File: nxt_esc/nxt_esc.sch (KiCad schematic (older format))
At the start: 15 parts, among them IC1 L293D, J1 NXT_MOTOR, J2 NXT_MOTOR, SW1 Skid Steer/Drive & Steer, U1 LM7809CT

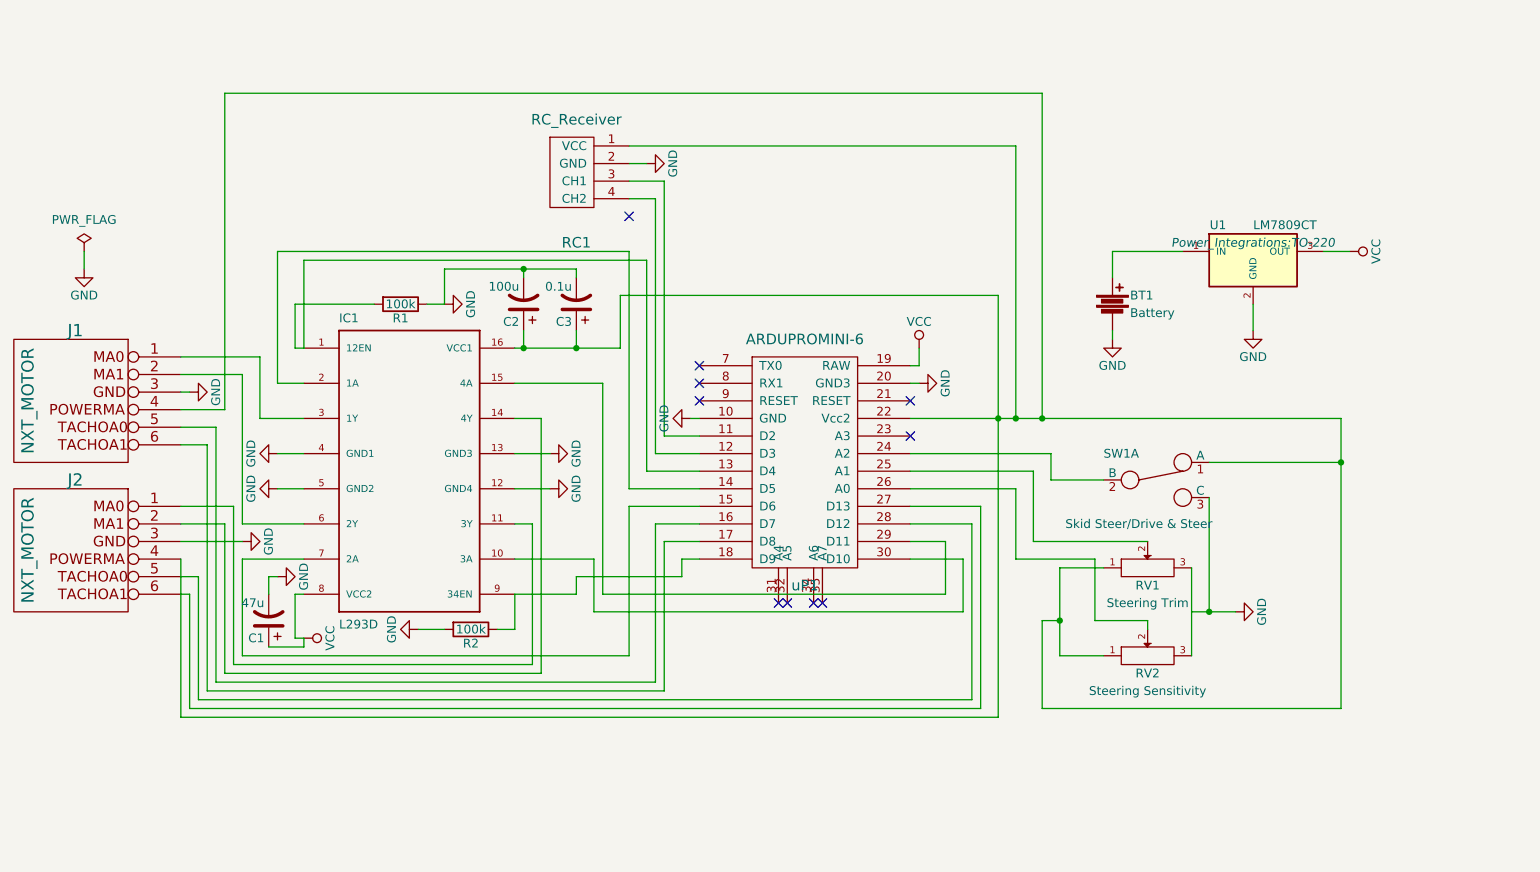
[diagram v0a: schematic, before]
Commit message: Changed schematic
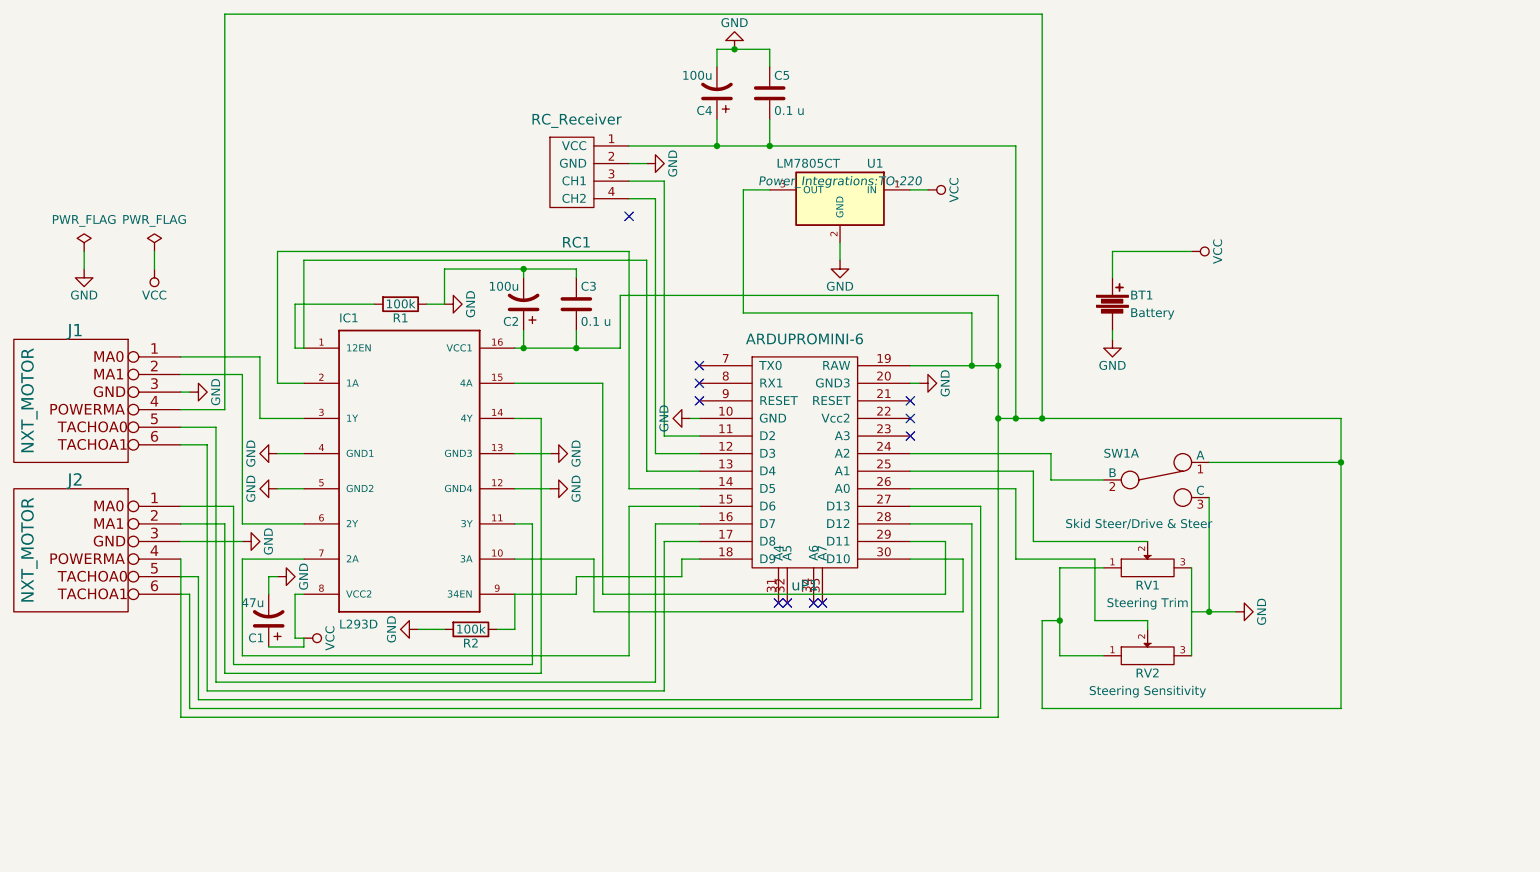
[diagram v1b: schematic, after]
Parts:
- removed C3: 0.1u, Capacitors_ThroughHole:C_Disc_D3.4mm_W2.1mm_P2.50mm, symbol CP1
- removed U1: LM7809CT, Power_Integrations:TO-220, symbol LM7809CT
- added C3, C5: 0.1 u, Capacitors_ThroughHole:C_Disc_D3.4mm_W2.1mm_P2.50mm, symbol C
- added C4: 100u, Capacitors_ThroughHole:CP_Radial_D5.0mm_P2.50mm, symbol CP1
- added U1: LM7805CT, Power_Integrations:TO-220, symbol LM7805CT
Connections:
- net GND: now also C3.1, C4.2, C5.1, U1.2 (GND)
- net VCC: now also BT1.1, U1.1 (IN); no longer uP1.19 (RAW)
- net at C2.1, IC1.16 (VCC1), J1.4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: now also uP1.19 (RAW), C3.2, C4.1, C5.2, U1.3 (OUT); no longer uP1.22 (Vcc2)
- no-connect marks 10 -> 11
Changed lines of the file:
@@
-$EndComp
-$Comp
-L VCC #PWR013
-U 1 1 5A555AFB
-P 6950 3000
-F 0 "#PWR013" H 6950 2850 50  0001 C CNN
-F 1 "VCC" H 6950 3150 50  0000 C CNN
-F 2 "" H 6950 3000 50  0000 C CNN
-F 3 "" H 6950 3000 50  0000 C CNN
-	1    6950 3000
-	1    0    0    -1
 $EndComp
 $Comp
@@
 $EndComp
 $Comp
-L GND #PWR014
+L GND #PWR013
 U 1 1 5A554FA2
 P 4250 2750
-F 0 "#PWR014" H 4250 2500 50  0001 C CNN
+F 0 "#PWR013" H 4250 2500 50  0001 C CNN
 F 1 "GND" H 4250 2600 50  0000 C CNN
 F 2 "" H 4250 2750 50  0000 C CNN
@@
 $EndComp
 $Comp
-L GND #PWR015
+L GND #PWR014
 U 1 1 5A5551A8
 P 4100 4600
-F 0 "#PWR015" H 4100 4350 50  0001 C CNN
+F 0 "#PWR014" H 4100 4350 50  0001 C CNN
 F 1 "GND" H 4100 4450 50  0000 C CNN
 F 2 "" H 4100 4600 50  0000 C CNN
@@
 $EndComp
 $Comp
-L GND #PWR016
+L GND #PWR015
 U 1 1 5A5557E8
 P 3300 4300
-F 0 "#PWR016" H 3300 4050 50  0001 C CNN
+F 0 "#PWR015" H 3300 4050 50  0001 C CNN
 F 1 "GND" H 3300 4150 50  0000 C CNN
 F 2 "" H 3300 4300 50  0000 C CNN
@@
 	-1   0    0    1
 $EndComp
-$Comp
-L CP1 C3
-U 1 1 5A555C2B
-P 5000 2750
-F 0 "C3" H 5025 2850 50  0000 L CNN
-F 1 "0.1u" H 5025 2650 50  0000 L CNN
-F 2 "Capacitors_ThroughHole:C_Disc_D3.4mm_W2.1mm_P2.50mm" H 5000 2750 50  0001 C CNN
-F 3 "" H 5000 2750 50  0000 C CNN
-	1    5000 2750
-	-1   0    0    1
-$EndComp
 Wire Wire Line
 	3450 3200 3300 3200
@@
 	3400 4400 3400 4650
 Wire Wire Line
-	6900 3100 6950 3100
-Wire Wire Line
-	6950 3100 6950 3000
-Wire Wire Line
 	2750 3350 3000 3350
 Wire Wire Line
-	3000 3350 3000 1550
-Wire Wire Line
-	3000 1550 7650 1550
-Wire Wire Line
-	7650 1550 7650 3400
+	3000 3350 3000 1100
+Wire Wire Line
+	3000 1100 7650 1100
+Wire Wire Line
+	7650 1100 7650 3400
 Wire Wire Line
 	2750 4200 2750 5100
@@
 Wire Wire Line
 	7400 2700 7400 5100
-Wire Wire Line
-	6900 3400 9350 3400
 Connection ~ 7400 3400
 Connection ~ 7500 3400
@@
 Connection ~ 4700 2550
 $Comp
-L LM7809CT U1
-U 1 1 5A556A7B
-P 8850 2500
-F 0 "U1" H 8650 2700 50  0000 C CNN
-F 1 "LM7809CT" H 8850 2700 50  0000 L CNN
-F 2 "Power_Integrations:TO-220" H 8850 2600 50  0000 C CIN
-F 3 "" H 8850 2500 50  0000 C CNN
-	1    8850 2500
-	1    0    0    -1
-$EndComp
-$Comp
-L VCC #PWR017
+L VCC #PWR016
 U 1 1 5A556AED
-P 9400 2450
-F 0 "#PWR017" H 9400 2300 50  0001 C CNN
-F 1 "VCC" H 9400 2600 50  0000 C CNN
-F 2 "" H 9400 2450 50  0000 C CNN
-F 3 "" H 9400 2450 50  0000 C CNN
-	1    9400 2450
+P 8500 2450
+F 0 "#PWR016" H 8500 2300 50  0001 C CNN
+F 1 "VCC" H 8500 2600 50  0000 C CNN
+F 2 "" H 8500 2450 50  0000 C CNN
+F 3 "" H 8500 2450 50  0000 C CNN
+	1    8500 2450
 	0    1    1    0
 $EndComp
-$Comp
-L GND #PWR018
-U 1 1 5A556B19
-P 8850 2900
-F 0 "#PWR018" H 8850 2650 50  0001 C CNN
-F 1 "GND" H 8850 2750 50  0000 C CNN
-F 2 "" H 8850 2900 50  0000 C CNN
-F 3 "" H 8850 2900 50  0000 C CNN
-	1    8850 2900
-	-1   0    0    -1
-$EndComp
-Wire Wire Line
-	8850 2750 8850 2900
-Wire Wire Line
-	9250 2450 9400 2450
 $Comp
 L Battery BT1
@@
 	1    0    0    -1
 $EndComp
-Wire Wire Line
-	8050 2600 8050 2450
-Wire Wire Line
-	8050 2450 8450 2450
-$Comp
-L GND #PWR019
+$Comp
+L GND #PWR017
 U 1 1 5A556F7B
 P 8050 2950
-F 0 "#PWR019" H 8050 2700 50  0001 C CNN
+F 0 "#PWR017" H 8050 2700 50  0001 C CNN
 F 1 "GND" H 8050 2800 50  0000 C CNN
 F 2 "" H 8050 2950 50  0000 C CNN
@@
 $EndComp
 $Comp
-L GND #PWR020
+L GND #PWR018
 U 1 1 5A55820D
 P 8750 4500
-F 0 "#PWR020" H 8750 4250 50  0001 C CNN
+F 0 "#PWR018" H 8750 4250 50  0001 C CNN
 F 1 "GND" H 8750 4350 50  0000 C CNN
 F 2 "" H 8750 4500 50  0000 C CNN
@@
 Connection ~ 9350 3650
 Connection ~ 7650 3400
+Wire Wire Line
+	8050 2600 8050 2450
+Wire Wire Line
+	8050 2450 8500 2450
+$Comp
+L LM7805CT U1
+U 1 1 5A56A755
+P 6500 2150
+F 0 "U1" H 6300 2350 50  0000 C CNN
+F 1 "LM7805CT" H 6500 2350 50  0000 L CNN
+F 2 "Power_Integrations:TO-220" H 6500 2250 50  0000 C CIN
+F 3 "" H 6500 2150 50  0000 C CNN
+	1    6500 2150
+	-1   0    0    -1
+$EndComp
+$Comp
+L GND #PWR019
+U 1 1 5A56A814
+P 6500 2500
+F 0 "#PWR019" H 6500 2250 50  0001 C CNN
+F 1 "GND" H 6500 2350 50  0000 C CNN
+F 2 "" H 6500 2500 50  0000 C CNN
+F 3 "" H 6500 2500 50  0000 C CNN
+	1    6500 2500
+	-1   0    0    -1
+$EndComp
+Wire Wire Line
+	6500 2400 6500 2500
+$Comp
+L VCC #PWR020
+U 1 1 5A56A933
+P 7000 2100
+F 0 "#PWR020" H 7000 1950 50  0001 C CNN
+F 1 "VCC" H 7000 2250 50  0000 C CNN
+F 2 "" H 7000 2100 50  0000 C CNN
+F 3 "" H 7000 2100 50  0000 C CNN
+	1    7000 2100
+	0    1    1    0
+$EndComp
+Wire Wire Line
+	6900 2100 7000 2100
+Wire Wire Line
+	6900 3100 7400 3100
+Wire Wire Line
+	5950 2800 5950 2100
+Wire Wire Line
+	5950 2100 6100 2100
+Wire Wire Line
+	5950 2800 7250 2800
+Wire Wire Line
+	7250 2800 7250 3100
+Wire Wire Line
+	9350 3400 7400 3400
+NoConn ~ 6900 3400
+Connection ~ 7400 3100
+Connection ~ 7250 3100
+$Comp
+L PWR_FLAG #FLG021
+U 1 1 5A56B6A2
+P 2600 2450
+F 0 "#FLG021" H 2600 2545 50  0001 C CNN
+F 1 "PWR_FLAG" H 2600 2630 50  0000 C CNN
+F 2 "" H 2600 2450 50  0000 C CNN
+F 3 "" H 2600 2450 50  0000 C CNN
+	1    2600 2450
+	1    0    0    -1
+$EndComp
+$Comp
+L VCC #PWR022
+U 1 1 5A56B6DA
+P 2600 2550
+F 0 "#PWR022" H 2600 2400 50  0001 C CNN
+F 1 "VCC" H 2600 2700 50  0000 C CNN
+F 2 "" H 2600 2550 50  0000 C CNN
+F 3 "" H 2600 2550 50  0000 C CNN
+	1    2600 2550
+	-1   0    0    1
+$EndComp
+Wire Wire Line
+	2600 2450 2600 2550
+$Comp
+L CP1 C4
+U 1 1 5A56BDA4
+P 5800 1550
+F 0 "C4" H 5825 1650 50  0000 L CNN
+F 1 "100u" H 5825 1450 50  0000 L CNN
+F 2 "Capacitors_ThroughHole:CP_Radial_D5.0mm_P2.50mm" H 5800 1550 50  0001 C CNN
+F 3 "" H 5800 1550 50  0000 C CNN
+	1    5800 1550
+	-1   0    0    1
+$EndComp
+Wire Wire Line
+	5800 1700 5800 1850
+Connection ~ 5800 1850
+Wire Wire Line
+	6100 1700 6100 1850
+Connection ~ 6100 1850
+$Comp
+L GND #PWR023
+U 1 1 5A56C0FF
+P 5900 1300
+F 0 "#PWR023" H 5900 1050 50  0001 C CNN
+F 1 "GND" H 5900 1150 50  0000 C CNN
+F 2 "" H 5900 1300 50  0000 C CNN
+F 3 "" H 5900 1300 50  0000 C CNN
+	1    5900 1300
+	1    0    0    1
+$EndComp
+Wire Wire Line
+	5800 1300 6100 1300
+Wire Wire Line
+	5800 1300 5800 1400
+Wire Wire Line
+	6100 1300 6100 1400
+Connection ~ 5900 1300
+$Comp
+L C C5
+U 1 1 5A56C39C
+P 6100 1550
+F 0 "C5" H 6125 1650 50  0000 L CNN
+F 1 "0.1 u" H 6125 1450 50  0000 L CNN
+F 2 "Capacitors_ThroughHole:C_Disc_D3.4mm_W2.1mm_P2.50mm" H 6138 1400 50  0001 C CNN
+F 3 "" H 6100 1550 50  0000 C CNN
+	1    6100 1550
+	1    0    0    -1
+$EndComp
+$Comp
+L C C3
+U 1 1 5A56C5FC
+P 5000 2750
+F 0 "C3" H 5025 2850 50  0000 L CNN
+F 1 "0.1 u" H 5025 2650 50  0000 L CNN
+F 2 "Capacitors_ThroughHole:C_Disc_D3.4mm_W2.1mm_P2.50mm" H 5038 2600 50  0001 C CNN
+F 3 "" H 5000 2750 50  0000 C CNN
+	1    5000 2750
+	1    0    0    -1
+$EndComp
 $EndSCHEMATC

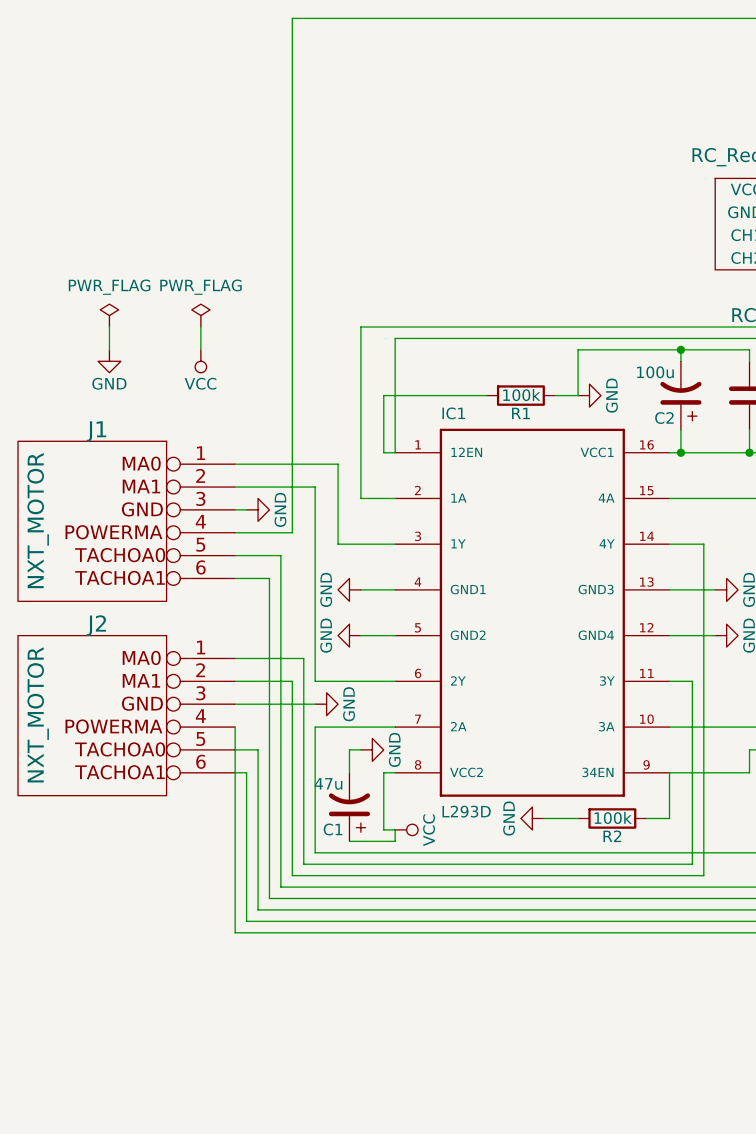
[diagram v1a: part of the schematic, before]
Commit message: Added smoothing capacitors
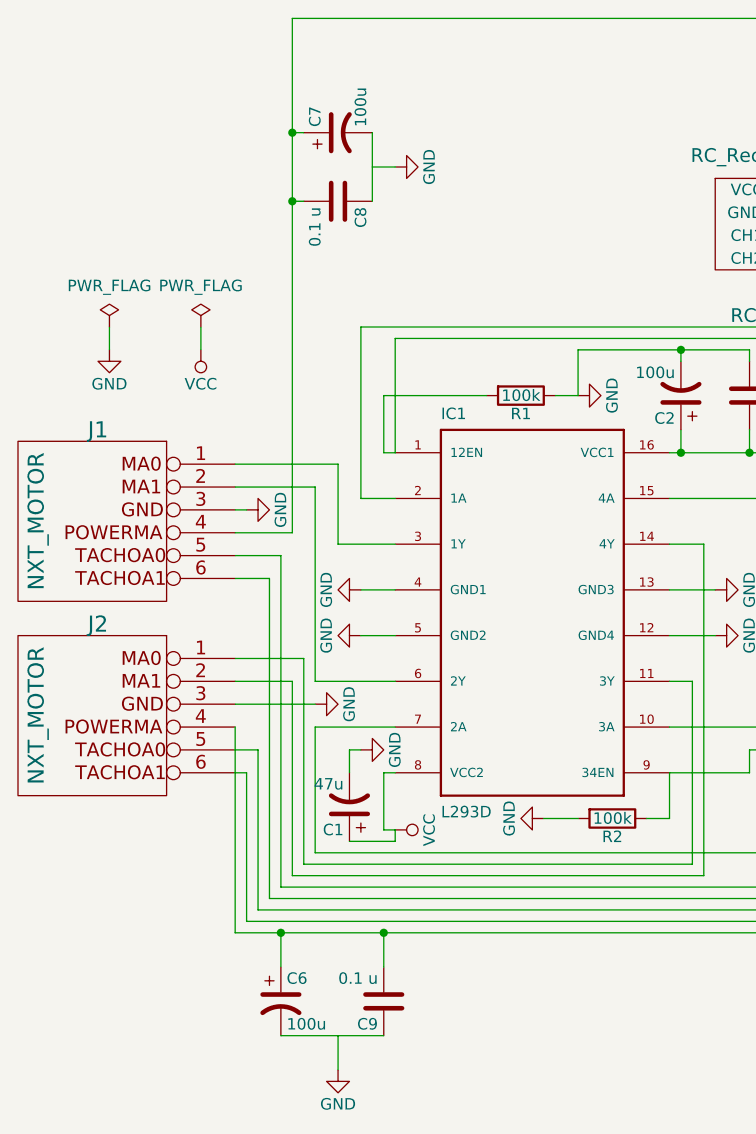
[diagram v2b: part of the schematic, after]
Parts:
- added C6, C7: 100u, Capacitors_ThroughHole:CP_Radial_D5.0mm_P2.50mm, symbol CP1
- added C8, C9: 0.1 u, Capacitors_ThroughHole:C_Disc_D3.4mm_W2.1mm_P2.50mm, symbol C
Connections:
- net at C2.1, C3.2, C4.1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: now also C6.1, C7.1, C8.2, C9.2
- new net: C7.2, C8.1
- new net: C6.2, C9.1
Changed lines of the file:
@@
 	1    0    0    -1
 $EndComp
+$Comp
+L CP1 C7
+U 1 1 5A56CDE0
+P 3200 1600
+F 0 "C7" H 3225 1700 50  0000 L CNN
+F 1 "100u" H 3225 1500 50  0000 L CNN
+F 2 "Capacitors_ThroughHole:CP_Radial_D5.0mm_P2.50mm" H 3200 1600 50  0001 C CNN
+F 3 "" H 3200 1600 50  0000 C CNN
+	1    3200 1600
+	0    -1   -1   0
+$EndComp
+$Comp
+L CP1 C6
+U 1 1 5A56CE66
+P 2950 5400
+F 0 "C6" H 2975 5500 50  0000 L CNN
+F 1 "100u" H 2975 5300 50  0000 L CNN
+F 2 "Capacitors_ThroughHole:CP_Radial_D5.0mm_P2.50mm" H 2950 5400 50  0001 C CNN
+F 3 "" H 2950 5400 50  0000 C CNN
+	1    2950 5400
+	1    0    0    -1
+$EndComp
+$Comp
+L C C8
+U 1 1 5A56CF0D
+P 3200 1900
+F 0 "C8" H 3225 2000 50  0000 L CNN
+F 1 "0.1 u" H 3225 1800 50  0000 L CNN
+F 2 "Capacitors_ThroughHole:C_Disc_D3.4mm_W2.1mm_P2.50mm" H 3238 1750 50  0001 C CNN
+F 3 "" H 3200 1900 50  0000 C CNN
+	1    3200 1900
+	0    1    1    0
+$EndComp
+$Comp
+L C C9
+U 1 1 5A56CF9D
+P 3400 5400
+F 0 "C9" H 3425 5500 50  0000 L CNN
+F 1 "0.1 u" H 3425 5300 50  0000 L CNN
+F 2 "Capacitors_ThroughHole:C_Disc_D3.4mm_W2.1mm_P2.50mm" H 3438 5250 50  0001 C CNN
+F 3 "" H 3400 5400 50  0000 C CNN
+	1    3400 5400
+	-1   0    0    1
+$EndComp
+$Comp
+L GND #PWR024
+U 1 1 5A56D05C
+P 3200 5700
+F 0 "#PWR024" H 3200 5450 50  0001 C CNN
+F 1 "GND" H 3200 5550 50  0000 C CNN
+F 2 "" H 3200 5700 50  0000 C CNN
+F 3 "" H 3200 5700 50  0000 C CNN
+	1    3200 5700
+	-1   0    0    -1
+$EndComp
+$Comp
+L GND #PWR025
+U 1 1 5A56D0A6
+P 3450 1750
+F 0 "#PWR025" H 3450 1500 50  0001 C CNN
+F 1 "GND" H 3450 1600 50  0000 C CNN
+F 2 "" H 3450 1750 50  0000 C CNN
+F 3 "" H 3450 1750 50  0000 C CNN
+	1    3450 1750
+	0    -1   1    0
+$EndComp
+Wire Wire Line
+	3350 1600 3350 1900
+Wire Wire Line
+	3350 1750 3450 1750
+Wire Wire Line
+	2950 5550 3400 5550
+Wire Wire Line
+	3200 5550 3200 5700
+Wire Wire Line
+	2950 5250 2950 5100
+Connection ~ 2950 5100
+Wire Wire Line
+	3400 5250 3400 5100
+Connection ~ 3400 5100
+Wire Wire Line
+	3050 1600 3000 1600
+Connection ~ 3000 1600
+Wire Wire Line
+	3050 1900 3000 1900
+Connection ~ 3000 1900
 $EndSCHEMATC
